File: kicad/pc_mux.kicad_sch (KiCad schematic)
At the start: 12 parts, among them U10 ATF22V10C-7PX, U3 ATF22V10C-10PU, U4 ATF22V10C-10PU, U7 ATF22V10C-7PX, U8 ATF22V10C-7PX, U9 ATF22V10C-7PX

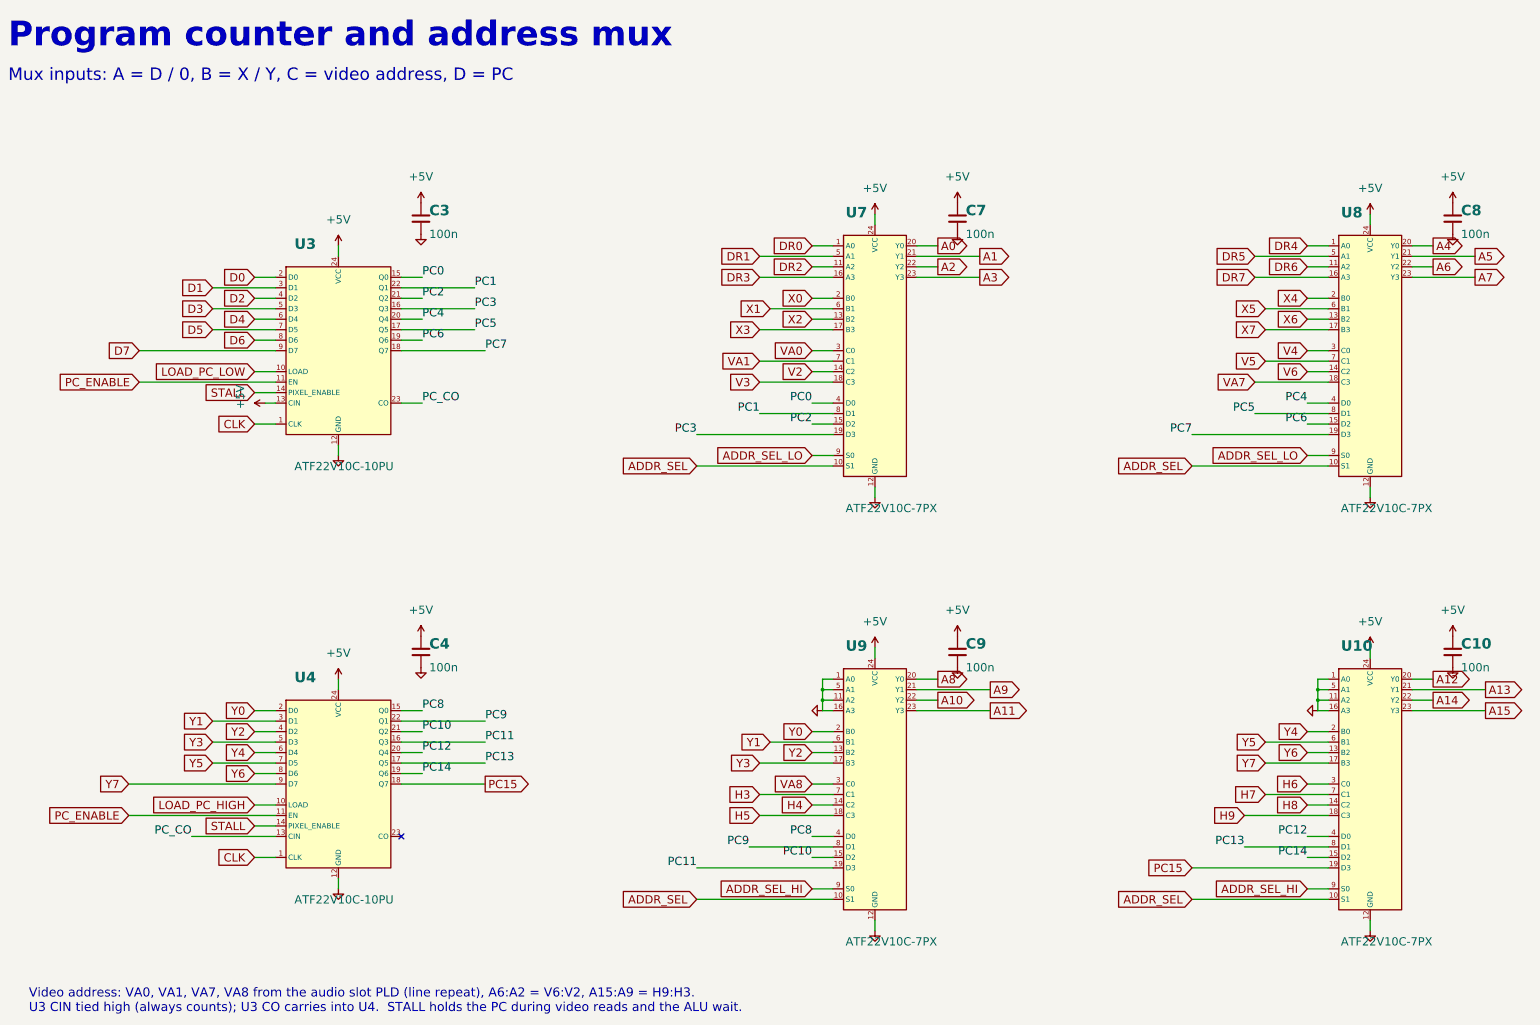
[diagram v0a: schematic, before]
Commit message: KiCad schematic: wire each sheet's nets, one routed bus per bus, PLD names
A net with two or more pins on a sheet is now wired pin to pin by a small
grid router (src/scripts/kicad_route.py) instead of a label per pin.
Numbered groups (D, A, SRC, PC, ...) are drawn as one bus per sheet with
bus entries, routed between the chips and named by one bus label.  Each
PLD shows its job under its part number.  Netlist check: 0 problems.

Co-Authored-By: Claude Opus 5.5 (1M context) <noreply@anthropic.com>
Claude-Session: https://claude.ai/code/session_01L9AkLuEg13EebxDmgXsaEp
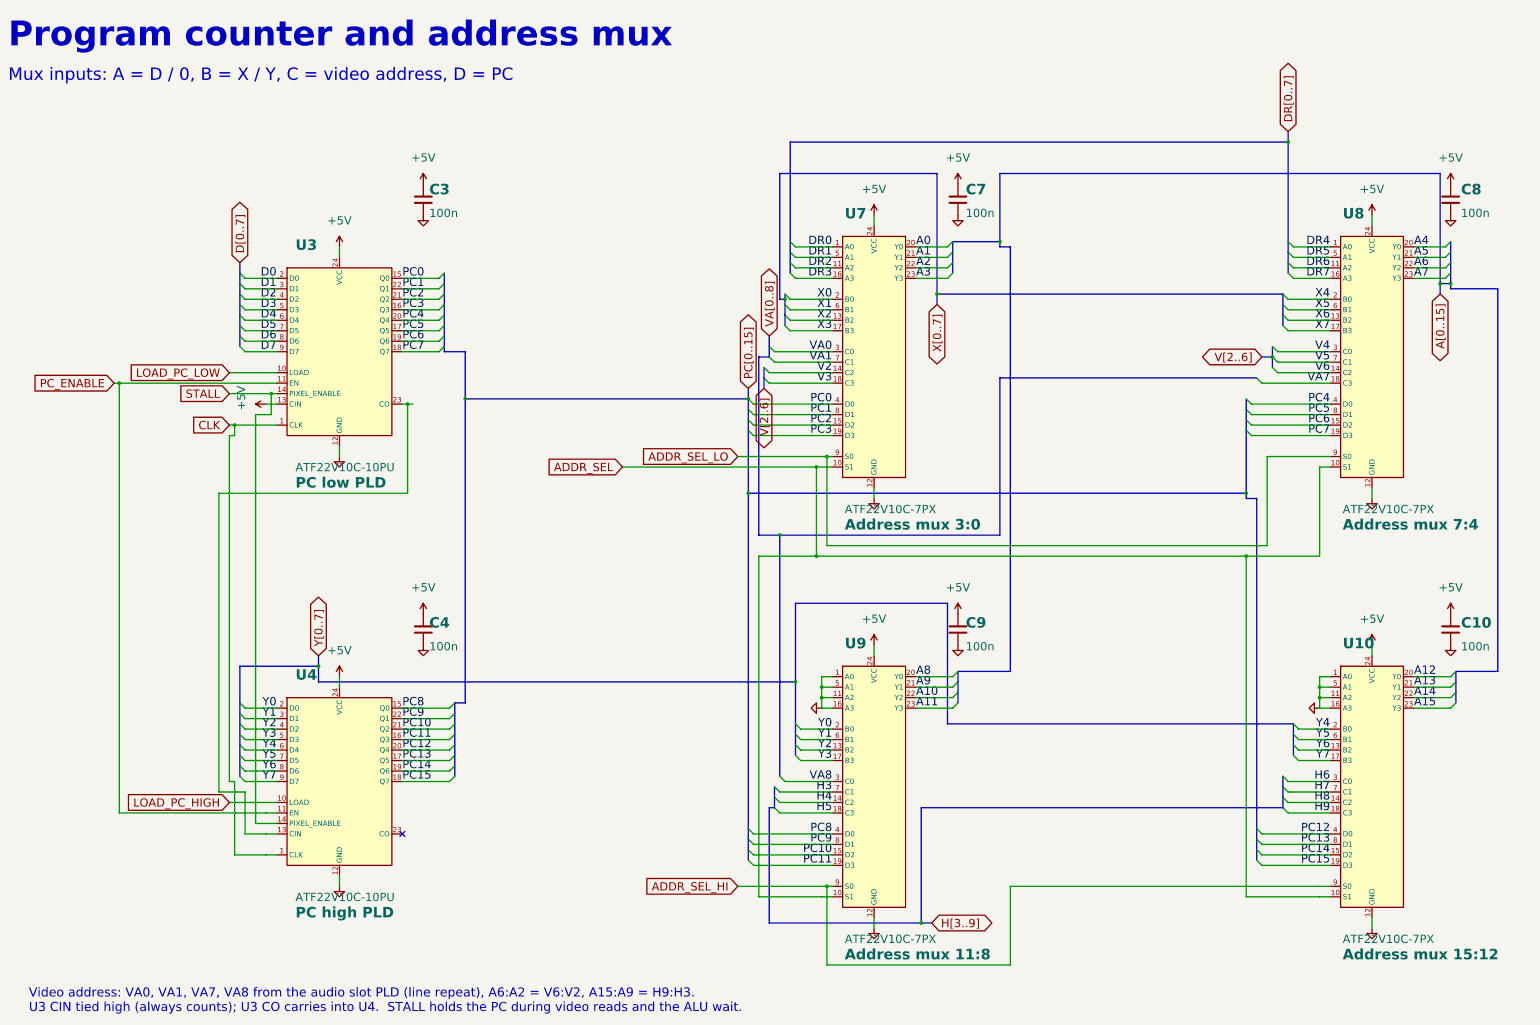
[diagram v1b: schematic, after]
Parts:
- U10: Function (none) -> Address mux 15:12
- U3: Function (none) -> PC low PLD
- U4: Function (none) -> PC high PLD
- U7: Function (none) -> Address mux 3:0
- U8: Function (none) -> Address mux 7:4
- U9: Function (none) -> Address mux 11:8
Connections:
- net PC_CO: no longer names the net of U3.23 (CO), U4.13 (CIN)

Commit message: Schematic: hand-placed video out sheet, larger pin text (work in progress)
The video and audio out sheet is laid out by hand like the PNG drawings:
straight PIX lines tapped onto the PIX bus, fanned RGB and DAC wires, the
ladder as a column.  KiCad's library parts are copied into placard_std with
larger pin text (gen_kicad_std.py); the PLD symbols' pin text is larger too.

Co-Authored-By: Claude Opus 5.5 (1M context) <noreply@anthropic.com>
Claude-Session: https://claude.ai/code/session_01L9AkLuEg13EebxDmgXsaEp
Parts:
- C10, C3, C4, C7, C8, C9: symbol Device:C -> placard_std:C
